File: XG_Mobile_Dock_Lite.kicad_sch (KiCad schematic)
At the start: 26 parts, among them J1 5-1775443-8, J13 1-1775099-3, J14 3-1775099-2, J17 8730, J2 20455-040E-76, J3 20455-040E-76, J4 3-2362375-4, J5 USB_C_Receptacle, SW1 SW_Push

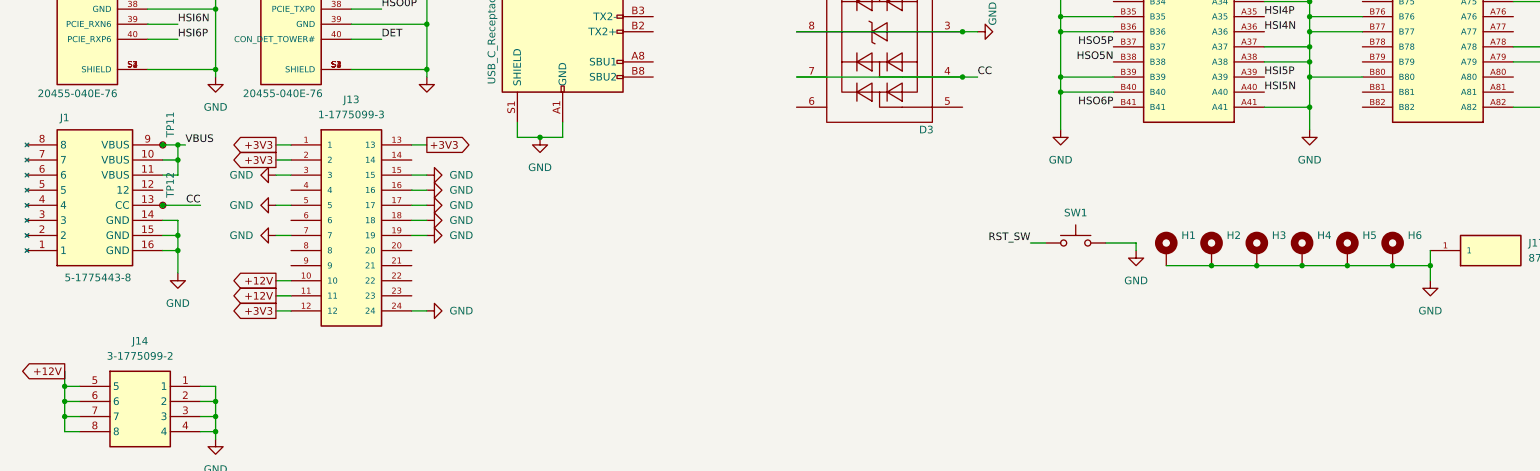
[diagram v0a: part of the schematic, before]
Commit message: pcb: redesign lite for the ADT-UT3G
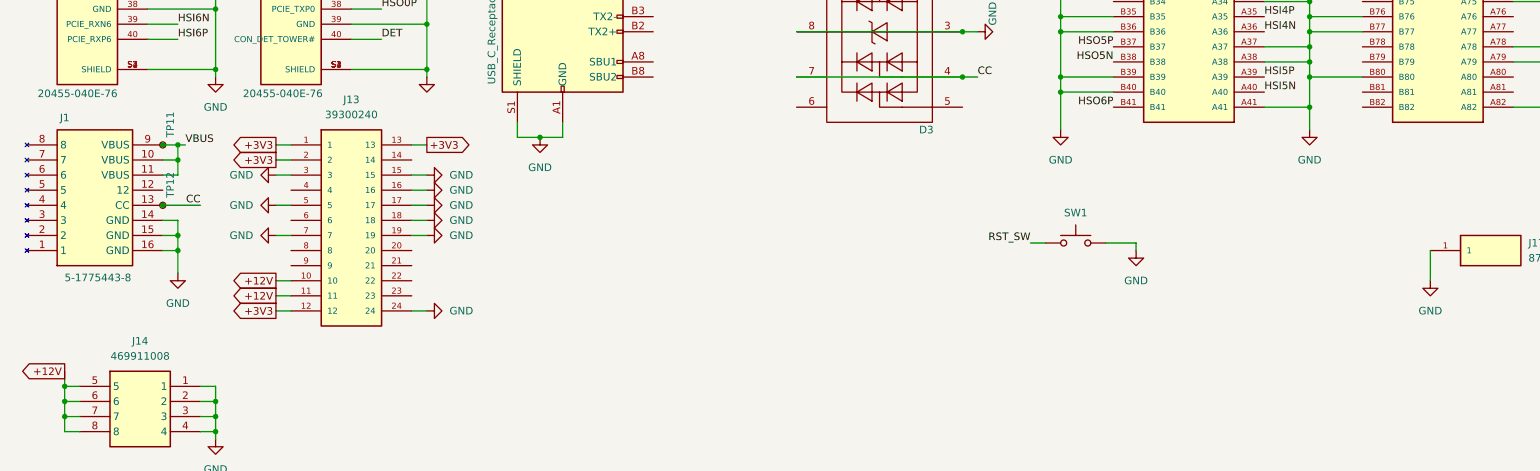
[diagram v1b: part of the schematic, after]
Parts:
- removed H1, H2, H3, H4, H5, H6: ~, XG_Mobile:Hole_200mil, symbol Mechanical:MountingHole_Pad
- J13: value 1-1775099-3 -> 39300240; footprint 1-1775099-3:1-1775099-3 -> 39300240:CON_39300240; Availability In Stock -> (none); Centerline_Pitch 4.2 mm[.165 in] -> (none); Check_prices https://www.snapeda.com/parts/1-1775099-3/TE+Connectivity+A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 -> (none); Comment 1-1775099-3 -> (none); Description_1 Conn Power PL 24 POS 4.2mm Solder ST Thru-Hole 24 Terminal 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 -> (none); LCSC C3250053 -> C492361; MANUFACTURER TE Connectivity -> (none); MF TE Connectivity -> (none); MP 1-1775099-3 -> (none); PARTREV G -> (none); Package None -> (none); Part_Number 1-1775099-3 -> 39300240; Price None -> (none); Product_Type Connector -> (none); STANDARD Manufacturer Recommendations -> (none); SnapEDA_Link https://www.snapeda.com/parts/1-1775099-3/TE+Connectivity+A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 -> (none)
- J14: value 3-1775099-2 -> 469911008; footprint 3-1775099-2:317750992 -> 469911008:CON_469911008; Height 13 -> (none); LCSC C17582043 -> C17470577; MANUFACTURER TE -> (none); Manufacturer_Name TE Connectivity -> (none); Manufacturer_Part_Number 3-1775099-2 -> (none); Mouser Part Number 571-3-1775099-2 -> (none); Mouser Price/Stock https://www.mouser.co.uk/ProductDetail/TE-Connectivity-AMP/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 -> (none); Part_Number 3-1775099-2 -> 469911008; STANDARD Manufacturer Recommendations -> (none)

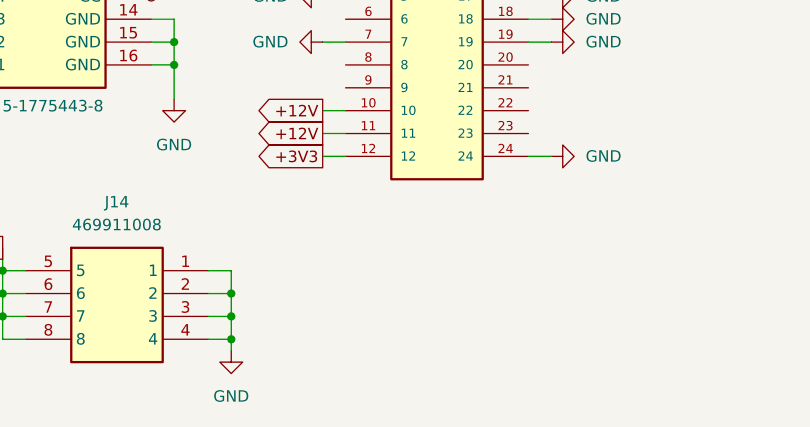
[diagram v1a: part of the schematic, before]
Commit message: pcb: add 12V pad for external fan connection
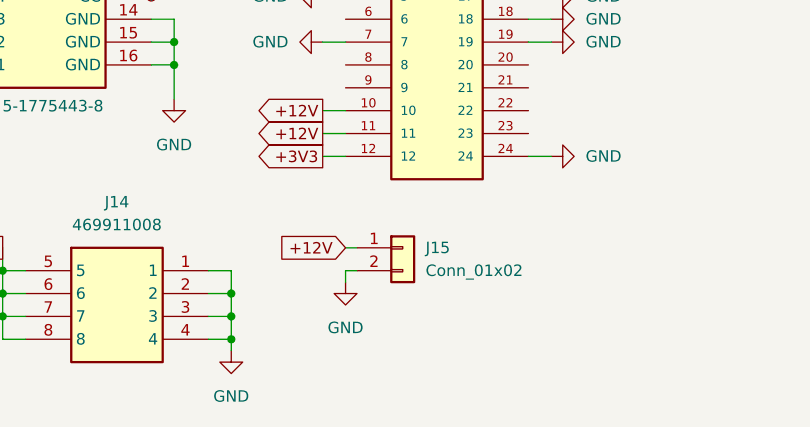
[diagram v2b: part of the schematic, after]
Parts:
- added J15: Conn_01x02, XG_Mobile:Solder_Pad_2P, symbol Connector_Generic:Conn_01x02
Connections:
- net +12V: now also J15.1 (Pin_1)
- net GND: now also J15.2 (Pin_2)
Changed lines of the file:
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@@
 	(wire
 		(pts
+			(xy 59.69 177.8) (xy 59.69 176.53)
+		)
+		(stroke
+			(width 0)
+			(type default)
+		)
+	)
+	(wire
+		(pts
 			(xy 189.23 99.06) (xy 189.23 106.68)
 		)
@@
 	(wire
 		(pts
+			(xy 59.69 173.99) (xy 60.96 173.99)
+		)
+		(stroke
+			(width 0)
+			(type default)
+		)
+	)
+	(wire
+		(pts
 			(xy 40.64 49.53) (xy 35.56 49.53)
 		)
@@
 	(wire
 		(pts
+			(xy 59.69 176.53) (xy 60.96 176.53)
+		)
+		(stroke
+			(width 0)
+			(type default)
+		)
+	)
+	(wire
+		(pts
 			(xy 172.72 78.74) (xy 175.26 78.74)
 		)
@@
 		)
 	)
+	(global_label "+12V"
+		(shape input)
+		(at 59.69 173.99 180)
+		(fields_autoplaced yes)
+		(effects
+			(font
+				(size 1.27 1.27)
+			)
+			(justify right)
+		)
+		(property "Intersheetrefs" "${INTERSHEET_REFS}"
+			(at 51.6248 173.99 0)
+			(effects
+				(font
+					(size 1.27 1.27)
+				)
+				(justify right)
+				(hide yes)
+			)
+		)
+	)
 	(global_label "+3V3"
 		(shape output)
@@
 	(symbol
 		(lib_id "power:GND")
+		(at 59.69 177.8 0)
+		(unit 1)
+		(exclude_from_sim no)
+		(in_bom yes)
+		(on_board yes)
+		(dnp no)
+		(fields_autoplaced yes)
+		(property "Reference" "#PWR017"
+			(at 59.69 184.15 0)
+			(effects
+				(font
+					(size 1.27 1.27)
+				)
+				(hide yes)
+			)
+		)
+		(property "Value" "GND"
+			(at 59.69 182.88 0)
+			(effects
+				(font
+					(size 1.27 1.27)
+				)
+			)
+		)
+		(property "Footprint" ""
+			(at 59.69 177.8 0)
+			(effects
+				(font
+					(size 1.27 1.27)
+				)
+				(hide yes)
+			)
+		)
+		(property "Datasheet" ""
+			(at 59.69 177.8 0)
+			(effects
+				(font
+					(size 1.27 1.27)
+				)
+				(hide yes)
+			)
+		)
+		(property "Description" "Power symbol creates a global label with name \"GND\" , ground"
+			(at 59.69 177.8 0)
+			(effects
+				(font
+					(size 1.27 1.27)
+				)
+				(hide yes)
+			)
+		)
+		(pin "1"
+		)
+		(instances
+			(project "XG_Mobile_Dock_Lite"
+				(path "/f97e6956-ab08-42cb-8fed-03fa58e87f0e"
+					(reference "#PWR017")
+					(unit 1)
+				)
+			)
+		)
+	)
+	(symbol
+		(lib_id "power:GND")
 		(at 101.6 39.37 0)
 		(unit 1)
@@
 					(unit 1)
 				)
+			)
+		)
+	)
+	(symbol
+		(lib_id "Connector_Generic:Conn_01x02")
+		(at 66.04 173.99 0)
+		(unit 1)
+		(exclude_from_sim no)
+		(in_bom no)
+		(on_board yes)
+		(dnp no)
+		(fields_autoplaced yes)
+		(property "Reference" "J15"
+			(at 68.58 173.9899 0)
+			(effects
+				(font
+					(size 1.27 1.27)
+				)
+				(justify left)
+			)
+		)
+		(property "Value" "Conn_01x02"
+			(at 68.58 176.5299 0)
+			(effects
+				(font
+					(size 1.27 1.27)
+				)
+				(justify left)
+			)
+		)
+		(property "Footprint" "XG_Mobile:Solder_Pad_2P"
+			(at 66.04 173.99 0)
+			(effects
+				(font
+					(size 1.27 1.27)
+				)
+				(hide yes)
+			)
+		)
+		(property "Datasheet" "~"
+			(at 66.04 173.99 0)
+			(effects
+				(font
+					(size 1.27 1.27)
+				)
+				(hide yes)
+			)
+		)
+		(property "Description" "Generic connector, single row, 01x02, script generated (kicad-library-utils/schlib/autogen/connector/)"
+			(at 66.04 173.99 0)
+			(effects
+				(font
+					(size 1.27 1.27)
+				)
+				(hide yes)
+			)
+		)
+		(pin "1"
+		)
+		(pin "2"
+		)
+		(instances
+			(project "XG_Mobile_Dock_Lite"
+				(path "/f97e6956-ab08-42cb-8fed-03fa58e87f0e"
+					(reference "J15")
+					(unit 1)
+				)

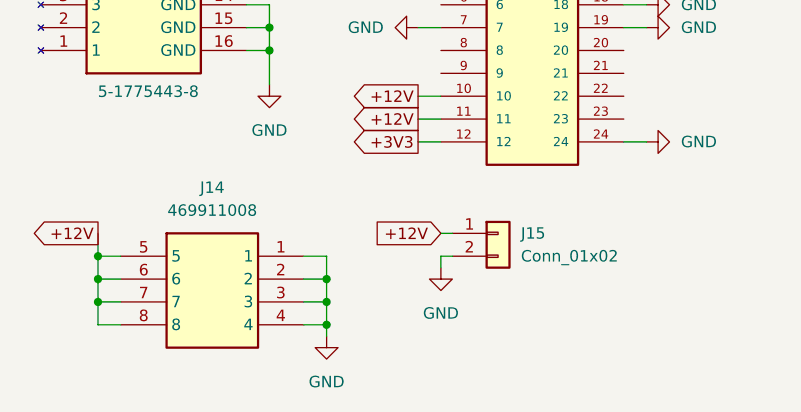
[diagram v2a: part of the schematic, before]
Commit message: pcb: add pwm fans to lite board
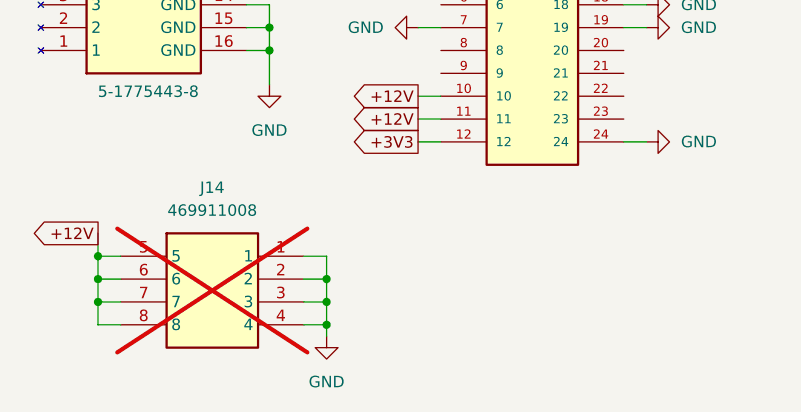
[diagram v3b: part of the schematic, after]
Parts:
- removed J15: Conn_01x02, XG_Mobile:Solder_Pad_2P, symbol Connector_Generic:Conn_01x02
- J14: now not fitted; now left out of the parts list
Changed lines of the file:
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@@
 	(wire
 		(pts
-			(xy 59.69 177.8) (xy 59.69 176.53)
-		)
-		(stroke
-			(width 0)
-			(type default)
-		)
-	)
-	(wire
-		(pts
 			(xy 189.23 99.06) (xy 189.23 106.68)
 		)
@@
 	(wire
 		(pts
-			(xy 59.69 173.99) (xy 60.96 173.99)
-		)
-		(stroke
-			(width 0)
-			(type default)
-		)
-	)
-	(wire
-		(pts
 			(xy 40.64 49.53) (xy 35.56 49.53)
 		)
@@
 	(wire
 		(pts
-			(xy 59.69 176.53) (xy 60.96 176.53)
-		)
-		(stroke
-			(width 0)
-			(type default)
-		)
-	)
-	(wire
-		(pts
 			(xy 172.72 78.74) (xy 175.26 78.74)
 		)
@@
 		)
 	)
-	(global_label "+12V"
-		(shape input)
-		(at 59.69 173.99 180)
-		(fields_autoplaced yes)
-		(effects
-			(font
-				(size 1.27 1.27)
-			)
-			(justify right)
-		)
-		(property "Intersheetrefs" "${INTERSHEET_REFS}"
-			(at 51.6248 173.99 0)
-			(effects
-				(font
-					(size 1.27 1.27)
-				)
-				(justify right)
-				(hide yes)
-			)
-		)
-	)
 	(global_label "+3V3"
 		(shape output)
@@
 	(symbol
 		(lib_id "power:GND")
-		(at 59.69 177.8 0)
-		(unit 1)
-		(exclude_from_sim no)
-		(in_bom yes)
-		(on_board yes)
-		(dnp no)
-		(fields_autoplaced yes)
-		(property "Reference" "#PWR017"
-			(at 59.69 184.15 0)
-			(effects
-				(font
-					(size 1.27 1.27)
-				)
-				(hide yes)
-			)
-		)
-		(property "Value" "GND"
-			(at 59.69 182.88 0)
-			(effects
-				(font
-					(size 1.27 1.27)
-				)
-			)
-		)
-		(property "Footprint" ""
-			(at 59.69 177.8 0)
-			(effects
-				(font
-					(size 1.27 1.27)
-				)
-				(hide yes)
-			)
-		)
-		(property "Datasheet" ""
-			(at 59.69 177.8 0)
-			(effects
-				(font
-					(size 1.27 1.27)
-				)
-				(hide yes)
-			)
-		)
-		(property "Description" "Power symbol creates a global label with name \"GND\" , ground"
-			(at 59.69 177.8 0)
-			(effects
-				(font
-					(size 1.27 1.27)
-				)
-				(hide yes)
-			)
-		)
-		(pin "1"
-		)
-		(instances
-			(project "XG_Mobile_Dock_Lite"
-				(path "/f97e6956-ab08-42cb-8fed-03fa58e87f0e"
-					(reference "#PWR017")
-					(unit 1)
-				)
-			)
-		)
-	)
-	(symbol
-		(lib_id "power:GND")
 		(at 101.6 39.37 0)
 		(unit 1)
@@
 		(unit 1)
 		(exclude_from_sim no)
-		(in_bom yes)
+		(in_bom no)
 		(on_board yes)
-		(dnp no)
+		(dnp yes)
 		(fields_autoplaced yes)
 		(property "Reference" "J14"
@@
 					(unit 1)
 				)
-			)
-		)
-	)
-	(symbol
-		(lib_id "Connector_Generic:Conn_01x02")
-		(at 66.04 173.99 0)
-		(unit 1)
-		(exclude_from_sim no)
-		(in_bom no)
-		(on_board yes)
-		(dnp no)
-		(fields_autoplaced yes)
-		(property "Reference" "J15"
-			(at 68.58 173.9899 0)
-			(effects
-				(font
-					(size 1.27 1.27)
-				)
-				(justify left)
-			)
-		)
-		(property "Value" "Conn_01x02"
-			(at 68.58 176.5299 0)
-			(effects
-				(font
-					(size 1.27 1.27)
-				)
-				(justify left)
-			)
-		)
-		(property "Footprint" "XG_Mobile:Solder_Pad_2P"
-			(at 66.04 173.99 0)
-			(effects
-				(font
-					(size 1.27 1.27)
-				)
-				(hide yes)
-			)
-		)
-		(property "Datasheet" "~"
-			(at 66.04 173.99 0)
-			(effects
-				(font
-					(size 1.27 1.27)
-				)
-				(hide yes)
-			)
-		)
-		(property "Description" "Generic connector, single row, 01x02, script generated (kicad-library-utils/schlib/autogen/connector/)"
-			(at 66.04 173.99 0)
-			(effects
-				(font
-					(size 1.27 1.27)
-				)
-				(hide yes)
-			)
-		)
-		(pin "1"
-		)
-		(pin "2"
-		)
-		(instances
-			(project "XG_Mobile_Dock_Lite"
-				(path "/f97e6956-ab08-42cb-8fed-03fa58e87f0e"
-					(reference "J15")
-					(unit 1)
-				)

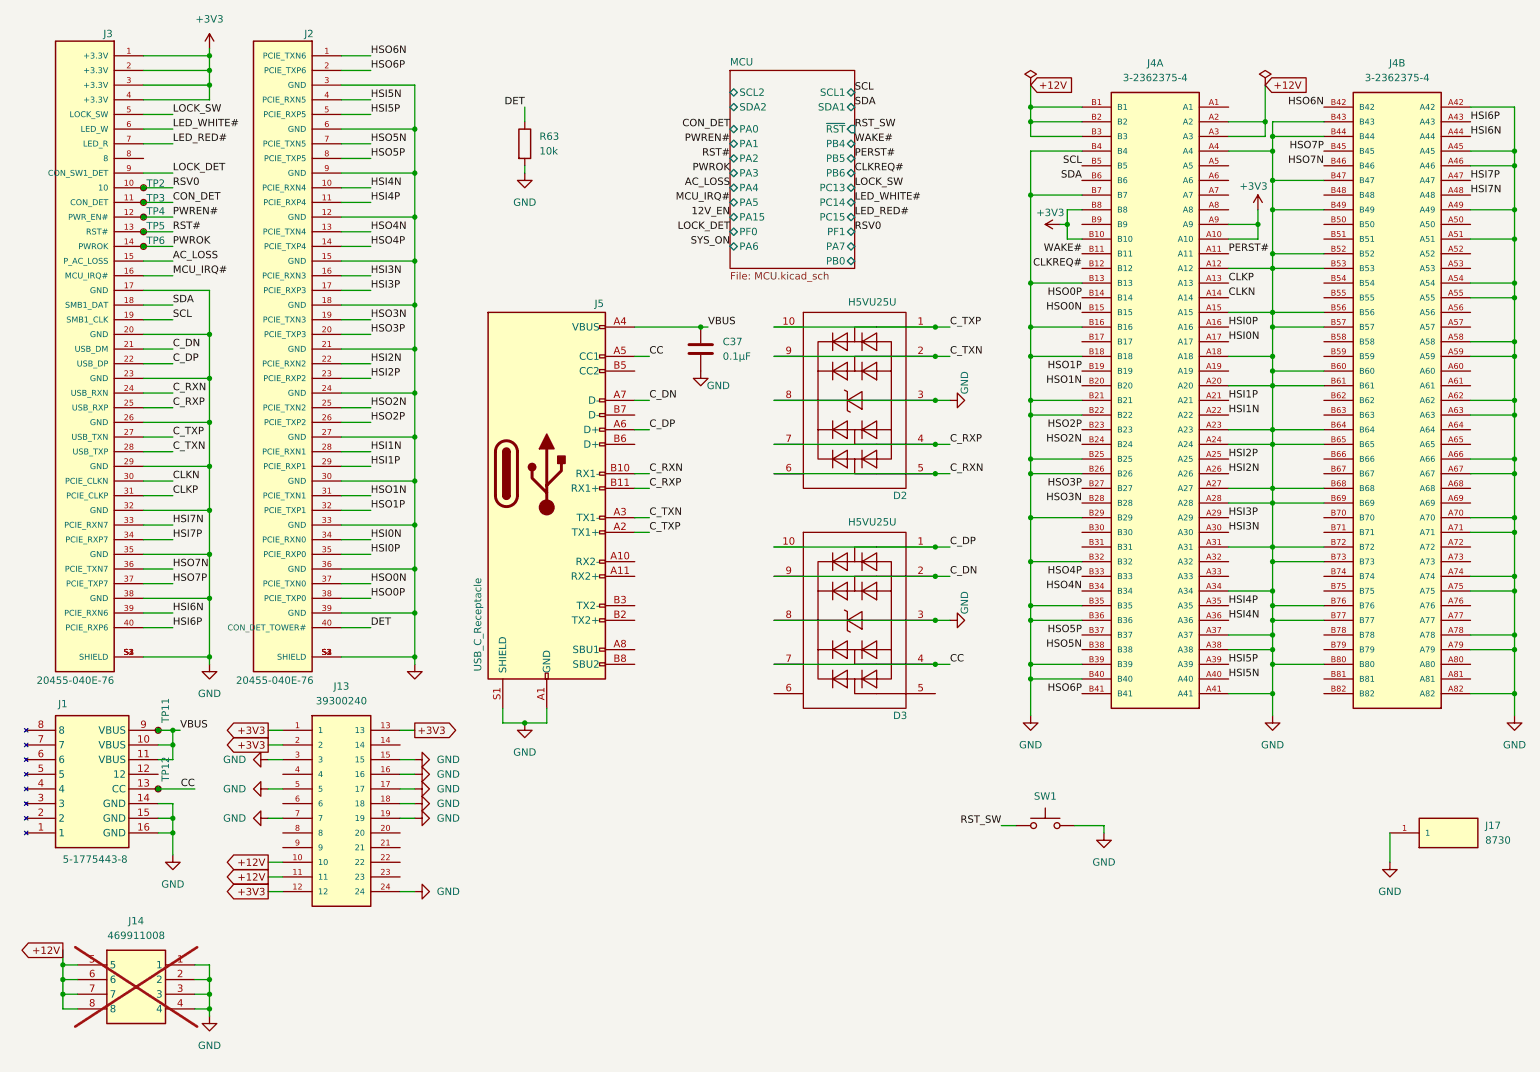
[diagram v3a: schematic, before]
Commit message: pcb: add PWON# and power LED to lite board
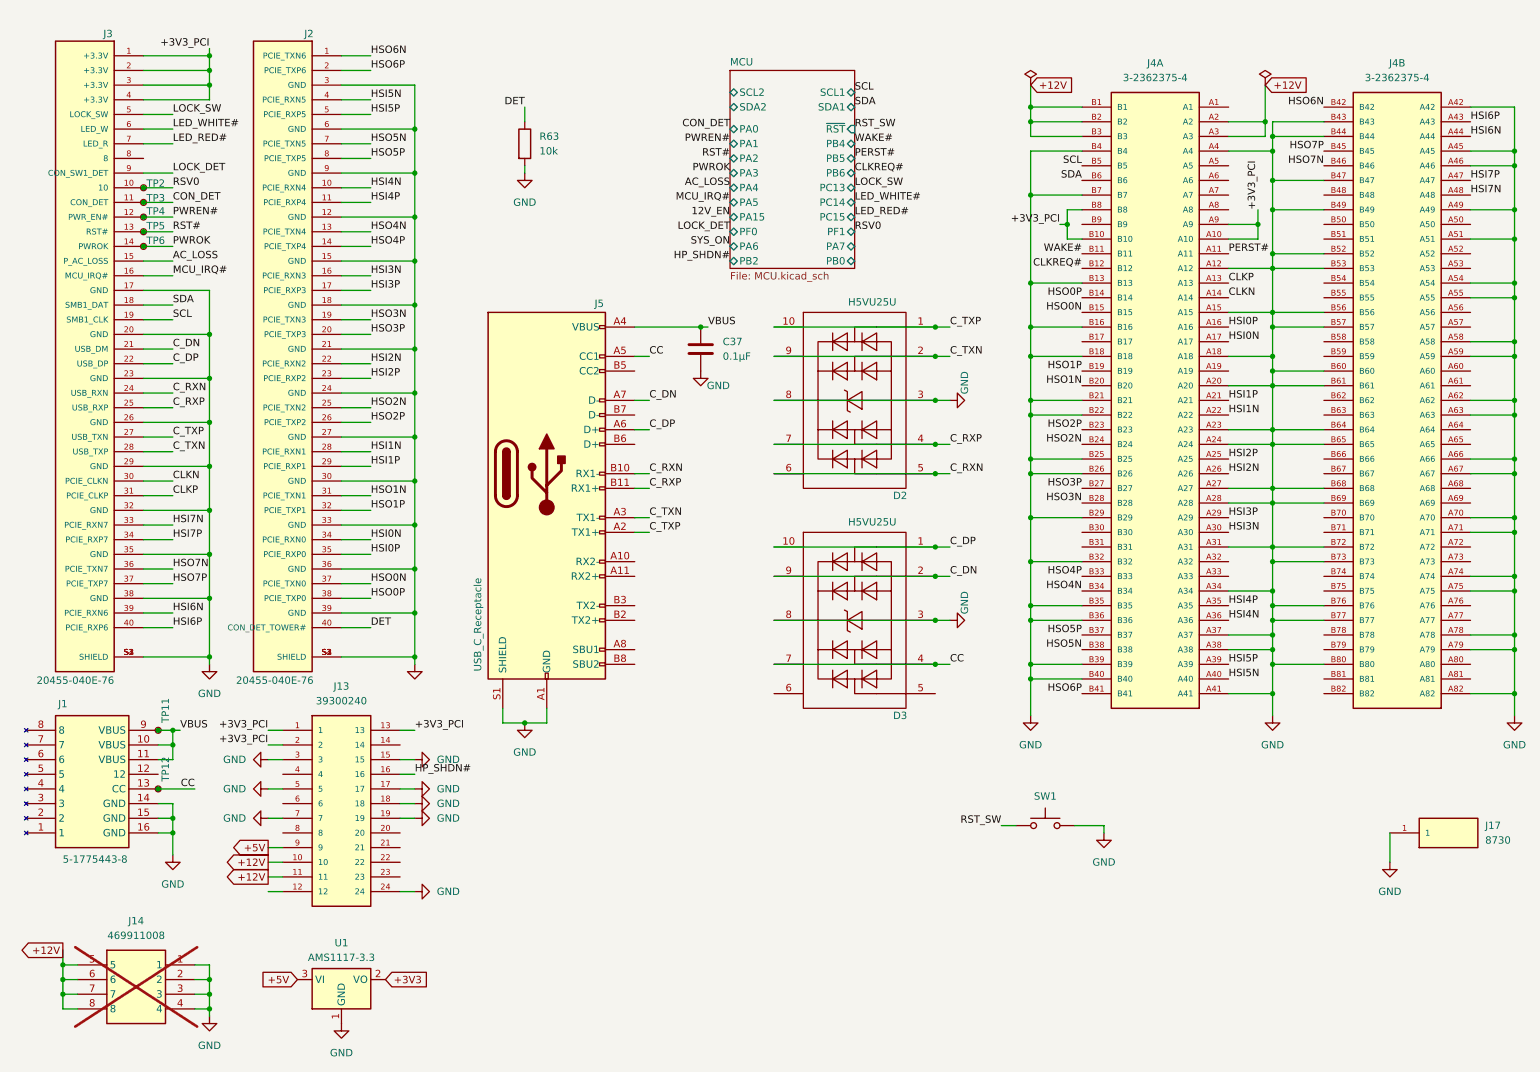
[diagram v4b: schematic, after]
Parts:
- added U1: AMS1117-3.3, Package_TO_SOT_SMD:SOT-223-3_TabPin2, symbol Regulator_Linear:AMS1117-3.3
- J13: LCSC C492361 -> C7541574; Part_Number 39300240 -> ZX-5557-4.2-2-12PWZ
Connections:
- net +3V3: now also U1.2 (VO); no longer J13.1, J13.12, J13.13, J13.2, J3.1 (+3.3V), J3.2 (+3.3V), J3.3 (+3.3V), J3.4 (+3.3V), J4.A10, J4.A9, J4.B10, J4.B8
- net GND: now also U1.1 (GND); no longer J13.16
- net +5V: now reaches J13.9
- net +5V: now also U1.3 (VI)
- new net +3V3_PCI: J13.1, J13.13, J13.2, J3.1 (+3.3V), J3.2 (+3.3V), J3.3 (+3.3V), J3.4 (+3.3V), J4.A10, J4.A9, J4.B10, J4.B8
- new net HP_SHDN#: J13.16
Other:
- sheet MCU ports: added PB2; removed none
